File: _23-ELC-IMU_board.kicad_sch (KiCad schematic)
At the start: 9 parts, among them J1 Deutsch DTM6, J2 Deutsch DTM6, J3 Conn_01x03

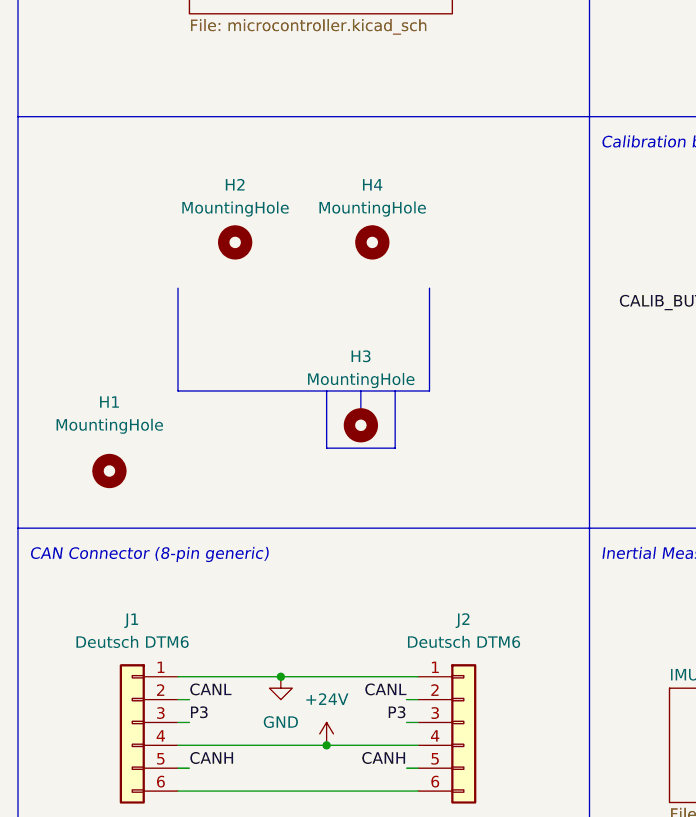
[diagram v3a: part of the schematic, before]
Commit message: Added DT connector footprints and began layout
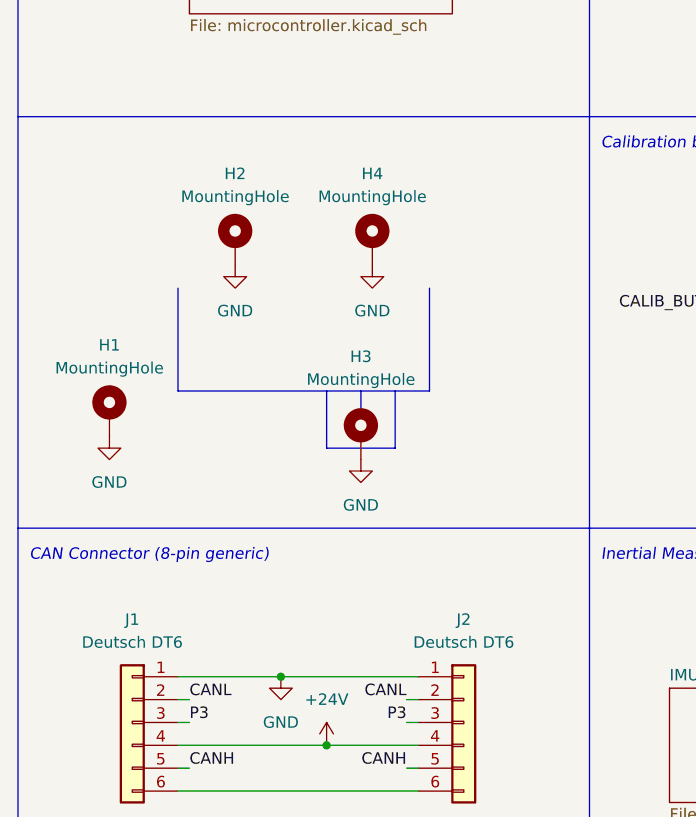
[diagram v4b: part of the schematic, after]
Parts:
- H1, H2, H3, H4: footprint (none) -> MountingHole:MountingHole_3.5mm_Pad; symbol Mechanical:MountingHole -> Mechanical:MountingHole_Pad
- J1, J2: value Deutsch DTM6 -> Deutsch DT6; footprint (none) -> Global Libraries:TE_DT15-6P
- J3: footprint (none) -> Connector_PinHeader_1.27mm:PinHeader_1x03_P1.27mm_Vertical_SMD_Pin1Left
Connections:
- net GND: now also H1.1, H2.1, H3.1, H4.1
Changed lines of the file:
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@@
     (in_bom yes) (on_board yes)
     (property "Reference" "J2" (id 0) (at 146.05 129.54 0))
-    (property "Value" "Deutsch DTM6" (id 1) (at 146.05 132.08 0))
-    (property "Footprint" "" (id 2) (at 146.05 140.97 0)
+    (property "Value" "Deutsch DT6" (id 1) (at 146.05 132.08 0))
+    (property "Footprint" "Global Libraries:TE_DT15-6P" (id 2) (at 146.05 140.97 0)
       (effects (font (size 1.27 1.27)) hide)
     )
@@
     (pin "1")
   )
-  (symbol (lib_id "Mechanical:MountingHole") (at 120.65 87.63 0) (unit 1)
+  (symbol (lib_id "power:GND") (at 134.62 111.76 0) (unit 1)
+    (in_bom yes) (on_board yes) (fields_autoplaced)
+    (property "Reference" "#PWR?" (id 0) (at 134.62 118.11 0)
+      (effects (font (size 1.27 1.27)) hide)
+    )
+    (property "Value" "GND" (id 1) (at 134.62 116.84 0))
+    (property "Footprint" "" (id 2) (at 134.62 111.76 0)
+      (effects (font (size 1.27 1.27)) hide)
+    )
+    (property "Datasheet" "" (id 3) (at 134.62 111.76 0)
+      (effects (font (size 1.27 1.27)) hide)
+    )
+    (pin "1")
+  )
+  (symbol (lib_id "power:GND") (at 135.89 90.17 0) (unit 1)
+    (in_bom yes) (on_board yes) (fields_autoplaced)
+    (property "Reference" "#PWR?" (id 0) (at 135.89 96.52 0)
+      (effects (font (size 1.27 1.27)) hide)
+    )
+    (property "Value" "GND" (id 1) (at 135.89 95.25 0))
+    (property "Footprint" "" (id 2) (at 135.89 90.17 0)
+      (effects (font (size 1.27 1.27)) hide)
+    )
+    (property "Datasheet" "" (id 3) (at 135.89 90.17 0)
+      (effects (font (size 1.27 1.27)) hide)
+    )
+    (pin "1")
+  )
+  (symbol (lib_id "Mechanical:MountingHole_Pad") (at 120.65 87.63 0) (unit 1)
     (in_bom yes) (on_board yes)
-    (property "Reference" "H2" (id 0) (at 120.65 81.28 0))
-    (property "Value" "MountingHole" (id 1) (at 120.65 83.82 0))
-    (property "Footprint" "" (id 2) (at 120.65 87.63 0)
+    (property "Reference" "H2" (id 0) (at 120.65 80.01 0))
+    (property "Value" "MountingHole" (id 1) (at 120.65 82.55 0))
+    (property "Footprint" "MountingHole:MountingHole_3.5mm_Pad" (id 2) (at 120.65 87.63 0)
       (effects (font (size 1.27 1.27)) hide)
     )
@@
       (effects (font (size 1.27 1.27)) hide)
     )
-  )
-  (symbol (lib_id "Mechanical:MountingHole") (at 135.89 87.63 0) (unit 1)
+    (pin "1")
+  )
+  (symbol (lib_id "Mechanical:MountingHole_Pad") (at 135.89 87.63 0) (unit 1)
     (in_bom yes) (on_board yes)
-    (property "Reference" "H4" (id 0) (at 135.89 81.28 0))
-    (property "Value" "MountingHole" (id 1) (at 135.89 83.82 0))
-    (property "Footprint" "" (id 2) (at 135.89 87.63 0)
+    (property "Reference" "H4" (id 0) (at 135.89 80.01 0))
+    (property "Value" "MountingHole" (id 1) (at 135.89 82.55 0))
+    (property "Footprint" "MountingHole:MountingHole_3.5mm_Pad" (id 2) (at 135.89 87.63 0)
       (effects (font (size 1.27 1.27)) hide)
     )
@@
       (effects (font (size 1.27 1.27)) hide)
     )
+    (pin "1")
   )
   (symbol (lib_id "power:+3V3") (at 110.49 45.72 0) (unit 1)
@@
       (effects (font (size 1.27 1.27)) (justify right))
     )
-    (property "Footprint" "" (id 2) (at 190.5 130.81 0)
+    (property "Footprint" "Connector_PinHeader_1.27mm:PinHeader_1x03_P1.27mm_Vertical_SMD_Pin1Left" (id 2) (at 190.5 130.81 0)
       (effects (font (size 1.27 1.27)) hide)
     )
@@
     (pin "3")
   )
-  (symbol (lib_id "Mechanical:MountingHole") (at 134.62 107.95 0) (unit 1)
+  (symbol (lib_id "Mechanical:MountingHole_Pad") (at 134.62 109.22 0) (unit 1)
     (in_bom yes) (on_board yes)
     (property "Reference" "H3" (id 0) (at 134.62 100.33 0))
     (property "Value" "MountingHole" (id 1) (at 134.62 102.87 0))
-    (property "Footprint" "" (id 2) (at 134.62 107.95 0)
-      (effects (font (size 1.27 1.27)) hide)
-    )
-    (property "Datasheet" "~" (id 3) (at 134.62 107.95 0)
-      (effects (font (size 1.27 1.27)) hide)
-    )
+    (property "Footprint" "MountingHole:MountingHole_3.5mm_Pad" (id 2) (at 134.62 109.22 0)
+      (effects (font (size 1.27 1.27)) hide)
+    )
+    (property "Datasheet" "~" (id 3) (at 134.62 109.22 0)
+      (effects (font (size 1.27 1.27)) hide)
+    )
+    (pin "1")
   )
   (symbol (lib_id "Connector_Generic:Conn_01x06") (at 109.22 140.97 0) (mirror y) (unit 1)
     (in_bom yes) (on_board yes) (fields_autoplaced)
     (property "Reference" "J1" (id 0) (at 109.22 129.54 0))
-    (property "Value" "Deutsch DTM6" (id 1) (at 109.22 132.08 0))
-    (property "Footprint" "" (id 2) (at 109.22 140.97 0)
+    (property "Value" "Deutsch DT6" (id 1) (at 109.22 132.08 0))
+    (property "Footprint" "Global Libraries:TE_DT15-6P" (id 2) (at 109.22 140.97 0)
       (effects (font (size 1.27 1.27)) hide)
     )
@@
     (pin "6")
   )
+  (symbol (lib_id "power:GND") (at 106.68 109.22 0) (unit 1)
+    (in_bom yes) (on_board yes) (fields_autoplaced)
+    (property "Reference" "#PWR?" (id 0) (at 106.68 115.57 0)
+      (effects (font (size 1.27 1.27)) hide)
+    )
+    (property "Value" "GND" (id 1) (at 106.68 114.3 0))
+    (property "Footprint" "" (id 2) (at 106.68 109.22 0)
+      (effects (font (size 1.27 1.27)) hide)
+    )
+    (property "Datasheet" "" (id 3) (at 106.68 109.22 0)
+      (effects (font (size 1.27 1.27)) hide)
+    )
+    (pin "1")
+  )
   (symbol (lib_id "Device:R") (at 180.34 101.6 0) (unit 1)
     (in_bom yes) (on_board yes) (fields_autoplaced)
@@
     (pin "1")
   )
-  (symbol (lib_id "Mechanical:MountingHole") (at 106.68 113.03 0) (unit 1)
+  (symbol (lib_id "Mechanical:MountingHole_Pad") (at 106.68 106.68 0) (unit 1)
     (in_bom yes) (on_board yes)
-    (property "Reference" "H1" (id 0) (at 106.68 105.41 0))
-    (property "Value" "MountingHole" (id 1) (at 106.68 107.95 0))
-    (property "Footprint" "" (id 2) (at 106.68 113.03 0)
-      (effects (font (size 1.27 1.27)) hide)
-    )
-    (property "Datasheet" "~" (id 3) (at 106.68 113.03 0)
-      (effects (font (size 1.27 1.27)) hide)
-    )
+    (property "Reference" "H1" (id 0) (at 106.68 99.06 0))
+    (property "Value" "MountingHole" (id 1) (at 106.68 101.6 0))
+    (property "Footprint" "MountingHole:MountingHole_3.5mm_Pad" (id 2) (at 106.68 106.68 0)
+      (effects (font (size 1.27 1.27)) hide)
+    )
+    (property "Datasheet" "~" (id 3) (at 106.68 106.68 0)
+      (effects (font (size 1.27 1.27)) hide)
+    )
+    (pin "1")
+  )
+  (symbol (lib_id "power:GND") (at 120.65 90.17 0) (unit 1)
+    (in_bom yes) (on_board yes) (fields_autoplaced)
+    (property "Reference" "#PWR?" (id 0) (at 120.65 96.52 0)
+      (effects (font (size 1.27 1.27)) hide)
+    )
+    (property "Value" "GND" (id 1) (at 120.65 95.25 0))
+    (property "Footprint" "" (id 2) (at 120.65 90.17 0)
+      (effects (font (size 1.27 1.27)) hide)
+    )
+    (property "Datasheet" "" (id 3) (at 120.65 90.17 0)
+      (effects (font (size 1.27 1.27)) hide)
+    )
+    (pin "1")
   )
   (symbol (lib_id "power:GND") (at 110.49 49.53 0) (unit 1)
@@
       (reference "#PWR051") (unit 1) (value "GND") (footprint "")
     )
+    (path "/27726f16-c541-41f6-a6cc-68d28f222a9a"
+      (reference "#PWR?") (unit 1) (value "GND") (footprint "")
+    )
+    (path "/33fe238c-4940-4821-8ef1-ac6acccc4c10"
+      (reference "#PWR?") (unit 1) (value "GND") (footprint "")
+    )
+    (path "/99dbf22c-1725-4fcf-8f3c-e2d774cf6ff3"
+      (reference "#PWR?") (unit 1) (value "GND") (footprint "")
+    )
+    (path "/f1939855-f981-4708-92f7-635e9536f1d1"
+      (reference "#PWR?") (unit 1) (value "GND") (footprint "")
+    )
     (path "/abd3ca57-2fe3-427b-95f1-6e678e3f0470/9b30c697-7dd3-4c25-8ced-516a5cbe8ad9"
-      (reference "C1") (unit 1) (value "100 nF") (footprint "Capacitor_SMD:C_0402_1005Metric")
+      (reference "C1") (unit 1) (value "100 nF") (footprint "Capacitor_SMD:C_0603_1608Metric")
     )
     (path "/abd3ca57-2fe3-427b-95f1-6e678e3f0470/f942c4ff-43d8-41ea-864e-a45291f037df"
-      (reference "C2") (unit 1) (value "100 nF") (footprint "Capacitor_SMD:C_0402_1005Metric")
+      (reference "C2") (unit 1) (value "100 nF") (footprint "Capacitor_SMD:C_0603_1608Metric")
     )
     (path "/54e69940-e60b-406d-b33c-8246d242800f/00000000-0000-0000-0000-00006343a469"
@@
     )
     (path "/ddcbeaef-7344-4f34-8775-b1d1f0415ae7"
-      (reference "H1") (unit 1) (value "MountingHole") (footprint "")
+      (reference "H1") (unit 1) (value "MountingHole") (footprint "MountingHole:MountingHole_3.5mm_Pad")
     )
     (path "/356ff616-b1b1-4416-9ded-9a91fb3271e6"
-      (reference "H2") (unit 1) (value "MountingHole") (footprint "")
+      (reference "H2") (unit 1) (value "MountingHole") (footprint "MountingHole:MountingHole_3.5mm_Pad")
     )
     (path "/8b54c01c-32c6-4484-b962-a405cc47c265"
-      (reference "H3") (unit 1) (value "MountingHole") (footprint "")
+      (reference "H3") (unit 1) (value "MountingHole") (footprint "MountingHole:MountingHole_3.5mm_Pad")
     )
     (path "/5a81ba6d-1cb8-4f90-ad37-c37491f7df47"
-      (reference "H4") (unit 1) (value "MountingHole") (footprint "")
+      (reference "H4") (unit 1) (value "MountingHole") (footprint "MountingHole:MountingHole_3.5mm_Pad")
     )
     (path "/98f8d048-5fd0-450e-921f-559b233f72a7"
-      (reference "J1") (unit 1) (value "Deutsch DTM6") (footprint "")
+      (reference "J1") (unit 1) (value "Deutsch DT6") (footprint "Global Libraries:TE_DT15-6P")
     )
     (path "/09bd8a18-fa7b-4015-8547-230d491cb9a1"
-      (reference "J2") (unit 1) (value "Deutsch DTM6") (footprint "")
+      (reference "J2") (unit 1) (value "Deutsch DT6") (footprint "Global Libraries:TE_DT15-6P")
     )
     (path "/5fe97024-2e49-4443-bc0c-2f1272ffe457"
-      (reference "J3") (unit 1) (value "Conn_01x03") (footprint "")
+      (reference "J3") (unit 1) (value "Conn_01x03") (footprint "Connector_PinHeader_1.27mm:PinHeader_1x03_P1.27mm_Vertical_SMD_Pin1Left")
     )
     (path "/54e69940-e60b-406d-b33c-8246d242800f/27fec5df-f50a-420e-8f18-082a387b0bca"

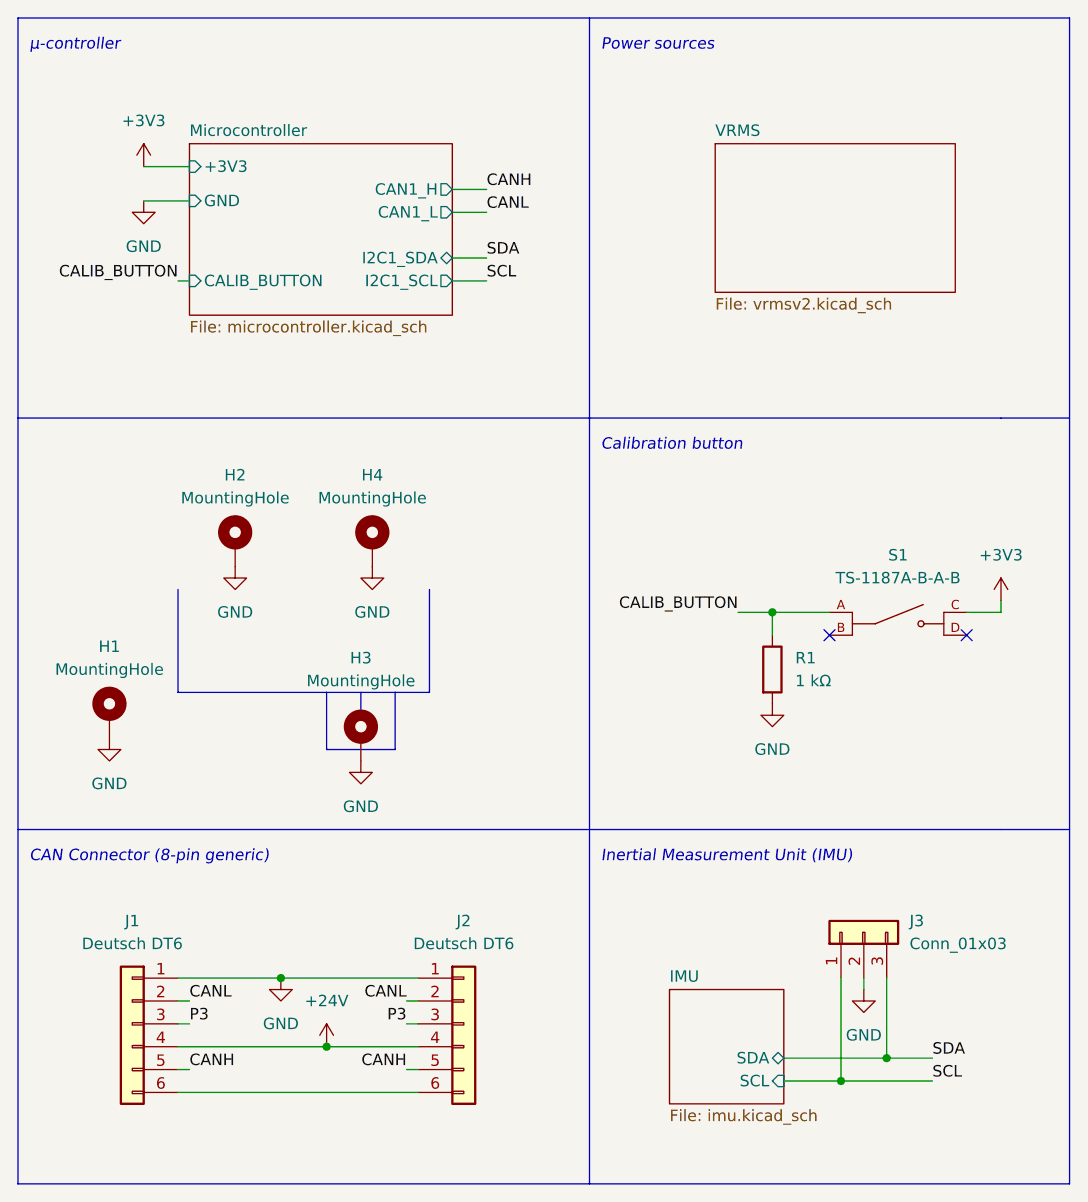
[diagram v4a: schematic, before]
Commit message: Added 0 Ω resistor to shield, grounded it, reannotated schematic, reassigned some footprints
Starting layout
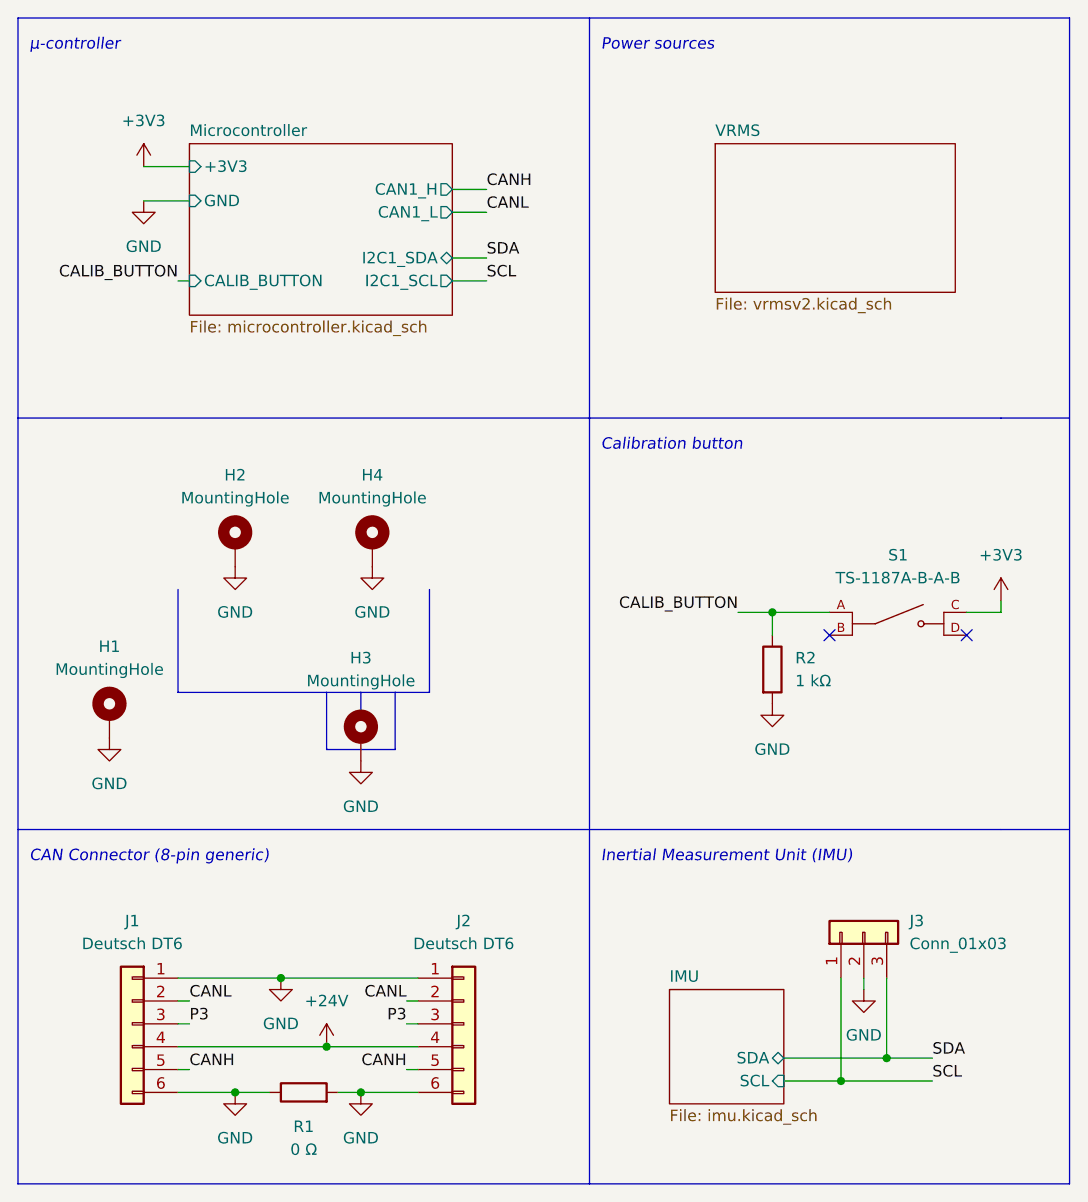
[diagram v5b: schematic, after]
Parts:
- added R1: 0 Ω, Resistor_SMD:R_0603_1608Metric_Pad0.98x0.95mm_HandSolder, symbol Device:R
- R2: renamed from R1; footprint Resistor_SMD:R_0201_0603Metric -> Resistor_SMD:R_0603_1608Metric_Pad0.98x0.95mm_HandSolder
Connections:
- net GND: now also J1.6 (Pin_6), J2.6 (Pin_6), R1.1, R1.2

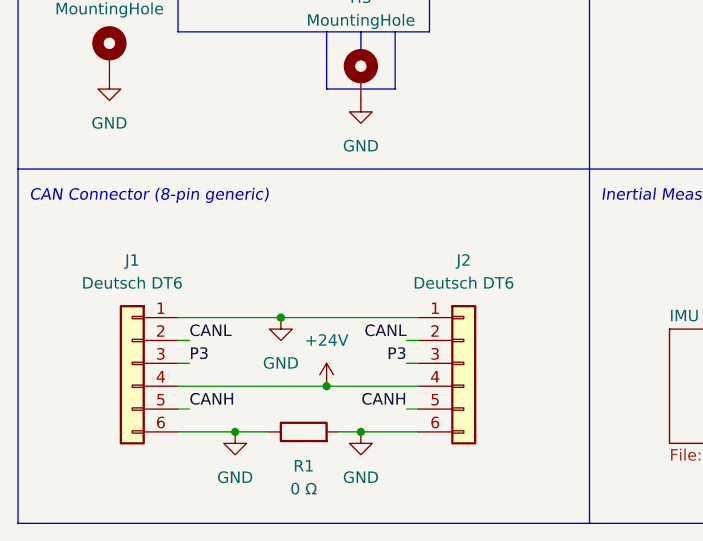
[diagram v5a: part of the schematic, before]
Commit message: Molex connectors wooo
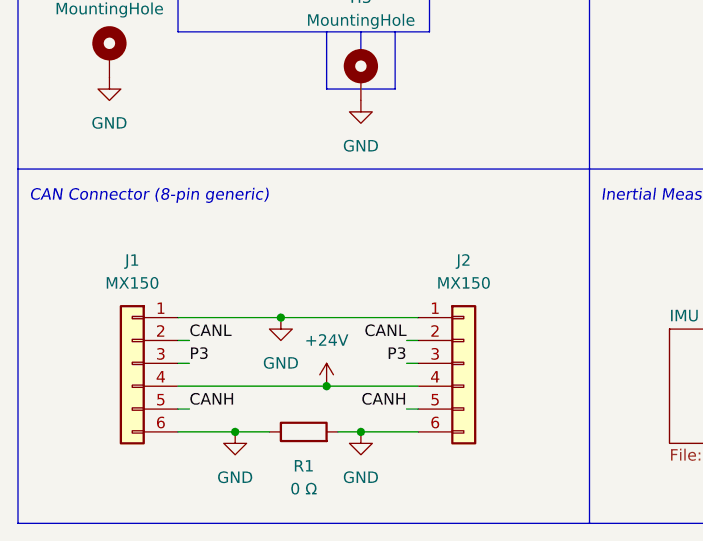
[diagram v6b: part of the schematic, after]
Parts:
- J1, J2: value Deutsch DT6 -> MX150; footprint Global Libraries:TE_DT15-6P -> Connector_Molex:Molex_Micro-Fit_3.0_43045-0600_2x03_P3.00mm_Horizontal
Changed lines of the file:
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@@
     (in_bom yes) (on_board yes)
     (property "Reference" "J2" (id 0) (at 146.05 129.54 0))
-    (property "Value" "Deutsch DT6" (id 1) (at 146.05 132.08 0))
-    (property "Footprint" "Global Libraries:TE_DT15-6P" (id 2) (at 146.05 140.97 0)
+    (property "Value" "MX150" (id 1) (at 146.05 132.08 0))
+    (property "Footprint" "Connector_Molex:Molex_Micro-Fit_3.0_43045-0600_2x03_P3.00mm_Horizontal" (id 2) (at 146.05 140.97 0)
       (effects (font (size 1.27 1.27)) hide)
     )
@@
     (in_bom yes) (on_board yes) (fields_autoplaced)
     (property "Reference" "J1" (id 0) (at 109.22 129.54 0))
-    (property "Value" "Deutsch DT6" (id 1) (at 109.22 132.08 0))
-    (property "Footprint" "Global Libraries:TE_DT15-6P" (id 2) (at 109.22 140.97 0)
+    (property "Value" "MX150" (id 1) (at 109.22 132.08 0))
+    (property "Footprint" "Connector_Molex:Molex_Micro-Fit_3.0_43045-0600_2x03_P3.00mm_Horizontal" (id 2) (at 109.22 140.97 0)
       (effects (font (size 1.27 1.27)) hide)
     )
@@
     )
     (path "/98f8d048-5fd0-450e-921f-559b233f72a7"
-      (reference "J1") (unit 1) (value "Deutsch DT6") (footprint "Global Libraries:TE_DT15-6P")
+      (reference "J1") (unit 1) (value "MX150") (footprint "Connector_Molex:Molex_Micro-Fit_3.0_43045-0600_2x03_P3.00mm_Horizontal")
     )
     (path "/09bd8a18-fa7b-4015-8547-230d491cb9a1"
-      (reference "J2") (unit 1) (value "Deutsch DT6") (footprint "Global Libraries:TE_DT15-6P")
+      (reference "J2") (unit 1) (value "MX150") (footprint "Connector_Molex:Molex_Micro-Fit_3.0_43045-0600_2x03_P3.00mm_Horizontal")
     )
     (path "/5fe97024-2e49-4443-bc0c-2f1272ffe457"
